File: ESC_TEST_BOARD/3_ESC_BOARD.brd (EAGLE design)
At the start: 119.2 x 68.1 mm, 63 parts, among them J3 AVR_SPI_PROG_3X2NS, U2 ATMEGA328P_TQFP

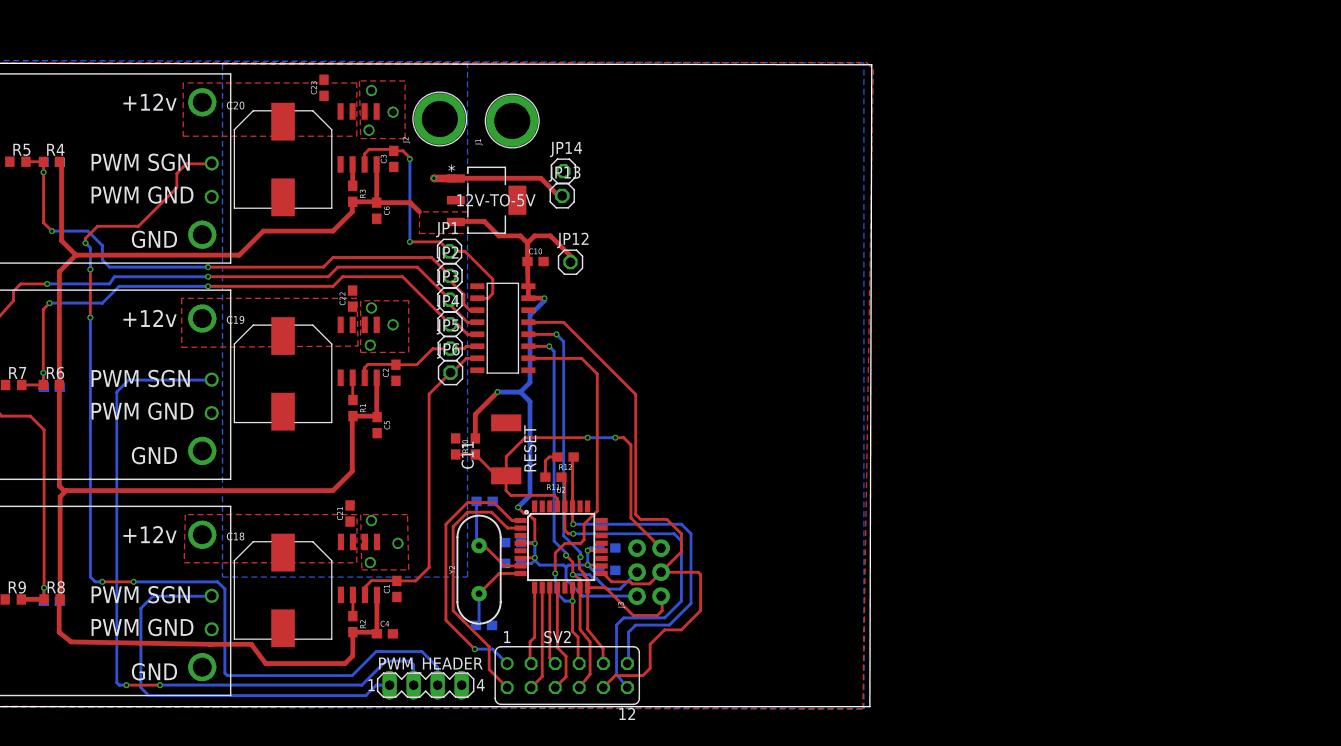
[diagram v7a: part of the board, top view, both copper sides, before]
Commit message: Finished adding the raspberry pi portion of the circuit board.
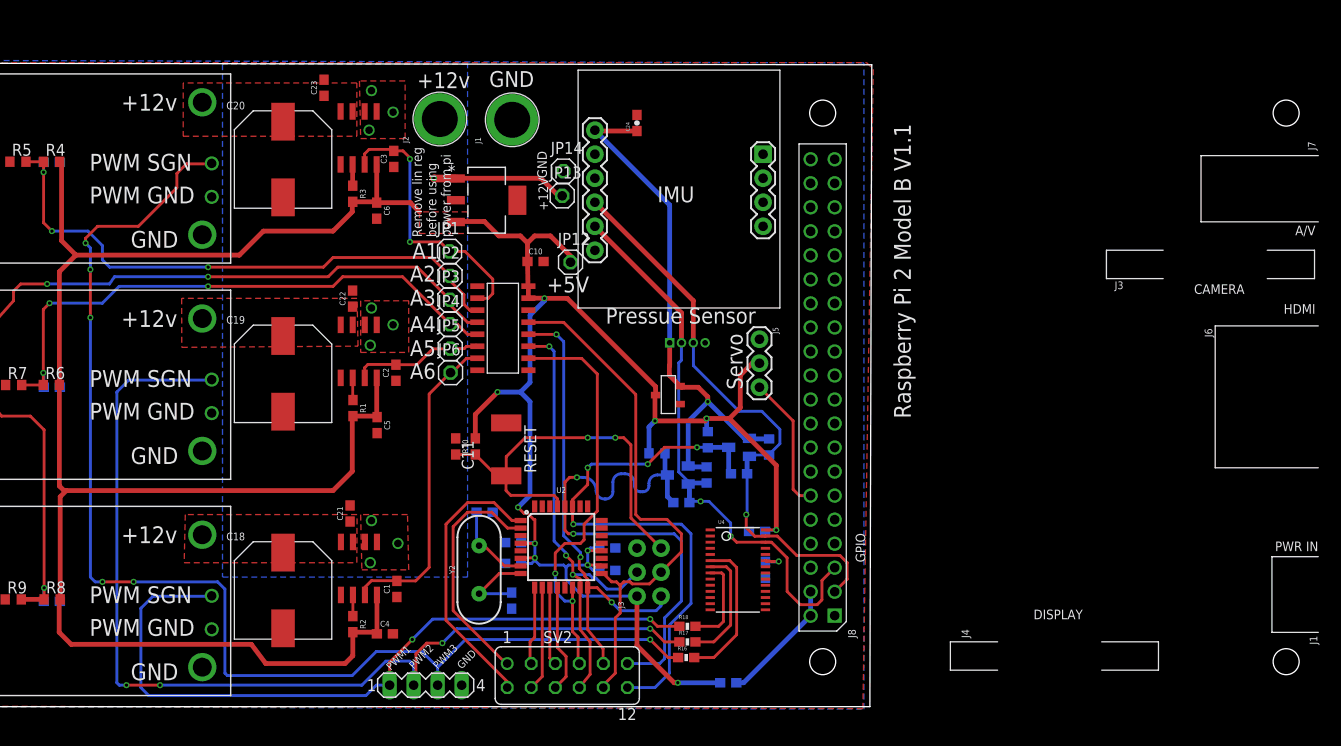
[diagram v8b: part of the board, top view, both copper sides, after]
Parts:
- removed R11, R12: (no value), SparkFun-Resistors:0603
- added C24: 0.1u, SparkFun-Passives:0603-CAP
- added C28: 10uF, SparkFun-Capacitors:0603-CAP
- added J5: (no value), SparkFun-Connectors:1X03
- added PCB1: RPI2, MicrocontrollerComponents:RPI2
- added PS: DF13-4P-1.25DSA, con-hirose-df13:DF13-4P-1.25DSA
- added R15: 10k, SparkFun-Resistors:0603-RES
- added R16, R17, R18: 0R, SparkFun-Resistors:0603-RES
- added R19, R25, R26: 0R, SparkFun-Passives:0603-RES
- added R21, R22, R23, R24: 10k, rcl:R0603
- added U$5: BNO055_9DOF_BREAKOUT, Other:BNO055
- added U$6, U$7: BSS138, BSS138:BSS138
- added U$8: AP2210, PowerComponents:SOT-23-3
- added U4: PCA9685, microbuilder:TSSOP28
- moved C17 3.94 mm to (81.4, 11.2), turned to 270 degrees
- moved C16 1.14 mm to (78.5, 20.6)
- moved J1 0.13 mm to (81.4, 62.1)
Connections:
- removed net +3V3: R11.2, R12.2
- new net 3.3V: C24.1, PS.P$1, R21.2, R23.2, U$5.VIN, U$6.G, U$7.G, U$8.VOUT
- new net N$35: R15.2, U4.23
- new net PWM_CON_0: R16.2, U4.6
- new net PWM_CON_1: R17.2, U4.7
- new net PWM_CON_10: U4.17
- new net PWM_CON_11: U4.18
- new net PWM_CON_12: U4.19
- new net PWM_CON_13: U4.20
- new net PWM_CON_14: U4.21
- new net PWM_CON_15: U4.22
- new net PWM_CON_2: R18.2, U4.8
- new net PWM_CON_3: U4.9
- new net PWM_CON_4: U4.10
- new net PWM_CON_5: U4.11
- new net PWM_CON_6: U4.12
- new net PWM_CON_7: U4.13
- new net PWM_CON_8: U4.15
- new net PWM_CON_9: U4.16
- new net RX: PCB1.P$10
- new net SCL_PI: PCB1.P$5, PS.P$2, R21.1, R26.1, U$5.SCL, U$6.S, U4.26
- new net SDA_PI: PCB1.P$3, PS.P$3, R23.1, R25.1, U$5.SDA, U$7.S, U4.27
- new net SERVO_PWM: J5.3, PCB1.P$12
- new net TX: PCB1.P$8
- new net VCC: PCB1.P$2, PCB1.P$4, R19.2
- net +5V: now also C28.1, J5.2, R19.1, R22.2, R24.2, U$8.VIN, U4.28
- net GND: now also C24.2, C28.2, J5.1, PCB1.P$14, PCB1.P$20, PCB1.P$25, PCB1.P$30, PCB1.P$34, PCB1.P$39, PCB1.P$6, PCB1.P$9, PS.P$4, R15.1, U$5.GND, U$8.GND, U4.1, U4.14, U4.2, U4.24, U4.25, U4.3, U4.4, U4.5
- net PD3: now also SV2.2; no longer SV2.1
- net PD4: now also SV2.1; no longer SV2.2
- net PWM1: now also R18.1
- net PWM2: now also R17.1
- net PWM3: now also R16.1
- net SCL: now also R22.1, R26.2, SV2.11, U$6.D; no longer R11.1, SV2.12
- net SDA: now also R24.1, R25.2, SV2.12, U$7.D; no longer R12.1, SV2.11
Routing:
- net +5V: track 272.7 -> 345.0 mm, vias 7 -> 11
- net SDA_PI: track 0.00 -> 62.4 mm, vias 0 -> 1
- net SCL_PI: track 0.00 -> 61.2 mm, vias 0 -> 2
- net 3.3V: track 0.00 -> 57.0 mm, vias 0 -> 1
- net PWM1: track 43.5 -> 78.8 mm, vias 0 -> 2
- net PWM2: track 76.2 -> 109.1 mm, vias 2 -> 4
- net PWM3: track 103.4 -> 130.8 mm, vias 5 -> 6
- net SDA: track 38.6 -> 59.4 mm, vias 1 -> 4
- net SCL: track 39.8 -> 56.2 mm, vias 1 -> 2
- net PWM_CON_0: track 0.00 -> 15.7 mm
- net SERVO_PWM: track 0.00 -> 14.4 mm
- net VCC: track 0.00 -> 13.3 mm
- net PWM_CON_1: track 0.00 -> 12.5 mm
- net SCK: track 68.3 -> 56.9 mm
- net PWM_CON_2: track 0.00 -> 9.59 mm
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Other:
- board text added: "+12V"
- board text added: "+12v"
- board text added: "+5V"
- board text added: "A1"
- board text added: "A2"
- board text added: "A3"
- board text added: "A4"
- board text added: "A5"
- board text added: "A6"
- board text added: "Bridge this to power system from rasp pi"
- board text added: "ESC Board Version1: 11/11/2017 Jacob Bobson Luke McBee Cynthia Zatlkowicz Grant Geyer Josh Burdine Melchor De La Garza"
- board text added: "GND"
- board text added: "IMU"
- board text added: "PWM1"
- board text added: "PWM2"
- board text added: "PWM3"
- board text added: "Pressue Sensor"
- board text added: "Remove lin reg before using power from pi"
- board text added: "Servo"
